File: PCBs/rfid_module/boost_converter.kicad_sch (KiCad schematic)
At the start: 8 parts, among them IC501 MAX17291BANT+T

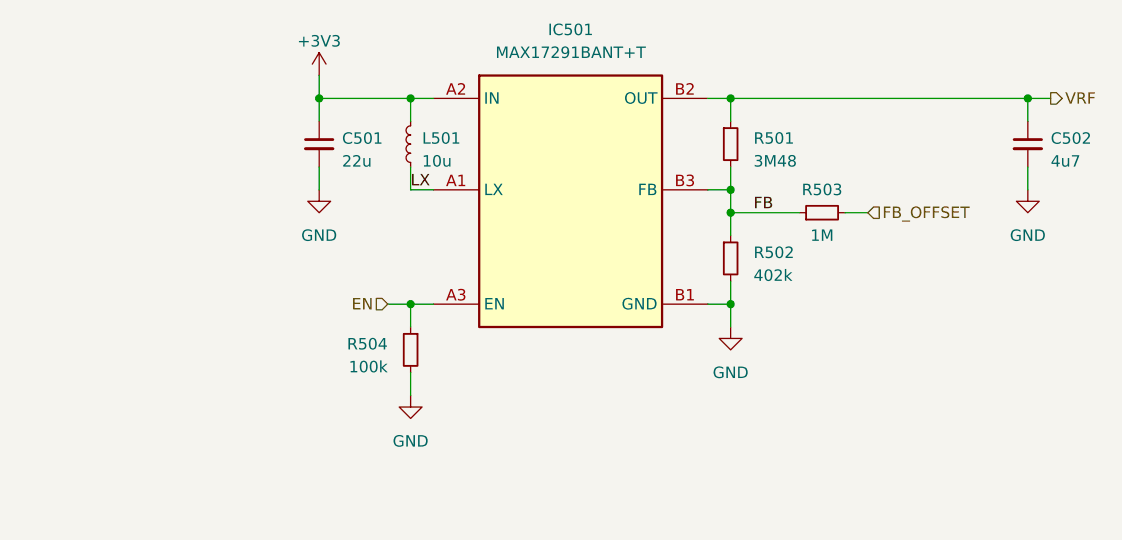
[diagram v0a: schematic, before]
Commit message: RFID PCB Done, started lower flex PCB
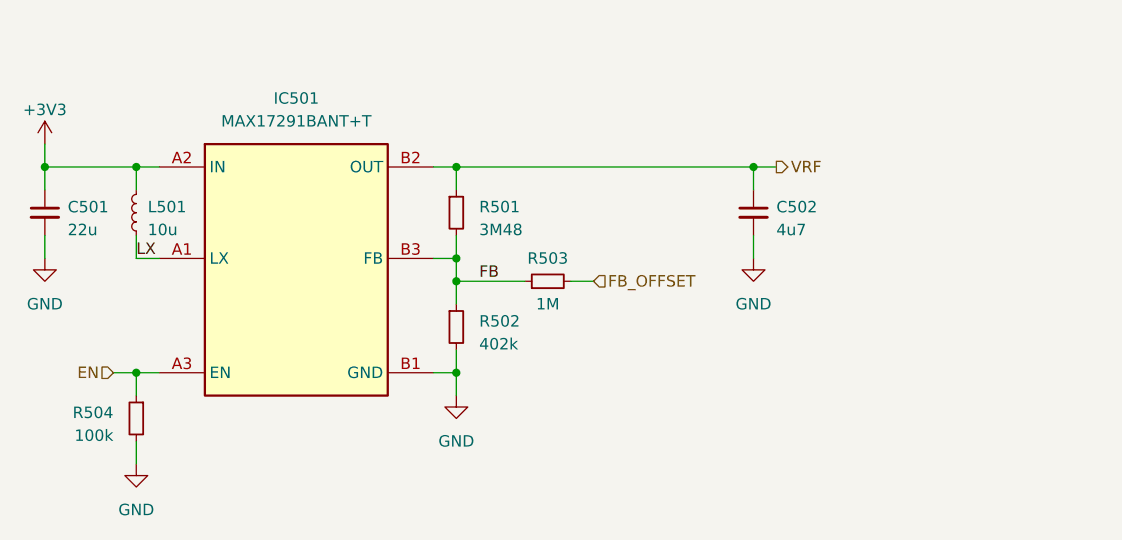
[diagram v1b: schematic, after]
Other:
- moved on the sheet: C501, C502, IC501, L501, R501, R502, R503, R504
